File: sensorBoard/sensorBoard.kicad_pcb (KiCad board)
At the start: 2 copper layers, 150 x 100 mm, 92 parts, among them J1 Conn_01x04, J2 Conn_01x02, J3 Conn_01x07, J4 Conn_01x04, J5 Conn_01x05, J6 Conn_01x02, J7 Conn_01x02, J8 Conn_01x03, K3 G2RL-1-H, K4 G2RL-1-H, Q1 NTD3055, Q2 2N7002, Q3 2SC4213, Q4 BSC440N10NS3G, Q5 BSC440N10NS3G, Q6 BSC440N10NS3G, Q7 BSC440N10NS3G, Q8 2N7002, Q9 2N7002, U1 STM32L476RGTx, U10 4N25, U11 4N25, U12 4011, U14 4011, U2 LD1117S33TR_SOT223, U3 MCP2551-I-SN, U4 LM75C, U6 4011, U7 BTS50080-1TEA, U8 4011, Y1 8MHz

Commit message: started to connect layout. added 0 Ohm resistors to separate the drivers.
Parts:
- added D7: ESD9B3.3ST5G, Diode_SMD:D_SOD-523, F.Cu at (79.0, 124.0)
- added R20: 0, Resistor_SMD:R_0805_2012Metric, F.Cu at (132.0, 53.2)
- added R21: 0, Resistor_SMD:R_0805_2012Metric, F.Cu at (132.1, 57.0)
- added R23: 0, Resistor_SMD:R_0805_2012Metric, F.Cu at (132.1, 60.3)
- added R24: 0, Resistor_SMD:R_0805_2012Metric, F.Cu at (132.1, 63.5)
- added R25: 0, Resistor_SMD:R_0805_2012Metric, F.Cu at (45.7, 75.0)
- added R30: 0, Resistor_SMD:R_0805_2012Metric, F.Cu at (64.2, 53.0)
- added R31: 0, Resistor_SMD:R_0805_2012Metric, F.Cu at (64.8, 79.5)
- added R32: 0, Resistor_SMD:R_0805_2012Metric, F.Cu at (77.2, 76.2)
- U10, U11: footprint Package_DIP:DIP-6_W7.62mm -> Package_DIP:SMDIP-6_W9.53mm_Clearance8mm
- moved U4 253.1 mm to (93.0, 104.0)
- moved Q3 247.8 mm to (92.0, 109.0)
- moved C4 242.7 mm to (98.0, 102.0)
- moved R2 240.5 mm to (101.0, 111.8)
- moved R3 240.4 mm to (96.9, 108.0)
- moved R1 240.1 mm to (101.0, 108.0), turned to 180 degrees
- moved R4 239.4 mm to (101.0, 115.5), turned to 180 degrees
- moved D8 235.3 mm to (58.0, 75.0), turned to 90 degrees
- moved R8 235.2 mm to (106.1, 100.0), turned to 180 degrees
- moved R10 234.3 mm to (106.0, 104.0), turned to 180 degrees
- moved R12 233.3 mm to (106.0, 108.0), turned to 180 degrees
- moved U13 232.5 mm to (116.0, 109.0)
- moved R9 232.5 mm to (110.0, 104.0), turned to 180 degrees
- moved R26 232.4 mm to (89.0, 88.0)
- moved R11 231.4 mm to (110.0, 108.0), turned to 180 degrees
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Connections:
- K3 pad 11: /Commutation/POLE+ -> /Commutation/Motor_driver_1/POLE1
- K4 pad 11: /Commutation/POLE- -> /Commutation/Motor_driver_1/POLE2
- Q4 pad 1: /Commutation/POLE+ -> /Commutation/Motor_driver_2/POLE_1
- Q4 pad 2: /Commutation/POLE+ -> /Commutation/Motor_driver_2/POLE_1
- Q4 pad 3: /Commutation/POLE+ -> /Commutation/Motor_driver_2/POLE_1
- Q5 pad 1: /Commutation/POLE- -> /Commutation/Motor_driver_2/POLE_2
- Q5 pad 2: /Commutation/POLE- -> /Commutation/Motor_driver_2/POLE_2
- Q5 pad 3: /Commutation/POLE- -> /Commutation/Motor_driver_2/POLE_2
- Q6 pad 5: /Commutation/POLE+ -> /Commutation/Motor_driver_2/POLE_1
- Q7 pad 5: /Commutation/POLE- -> /Commutation/Motor_driver_2/POLE_2
- U12 pad 10: unconnected-(U12-Pad10) -> Net-(U12-Pad10)
- U12 pad 12: Net-(U12-Pad12) -> Net-(U12-Pad10)
- U12 pad 13: Net-(U12-Pad12) -> Net-(U12-Pad10)
- U12 pad 14: +5V -> +12V
- U12 pad 8: unconnected-(U12-Pad8) -> Net-(U12-Pad3)
- U12 pad 9: unconnected-(U12-Pad9) -> Net-(U15-2Y)
- U14 pad 10: Net-(U12-Pad12) -> unconnected-(U14-Pad10)
- U14 pad 14: +5V -> +12V
- U14 pad 8: Net-(U12-Pad3) -> unconnected-(U14-Pad8)
- U14 pad 9: Net-(U15-2Y) -> unconnected-(U14-Pad9)
- U15 pad 1: /DIN -> /Commutation/Motor_driver_1/DIN
- U15 pad 3: /EN_MOTOR -> /Commutation/Motor_driver_1/EN_MOTOR
- U5 pad 1: /DIN -> /Commutation/Motor_driver_2/DIN
- U5 pad 3: /EN_MOTOR -> /Commutation/Motor_driver_2/EN_MOTOR
- U6 pad 14: +5V -> +12V
- U8 pad 14: +5V -> +12V
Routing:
- net Net-(U5-2Y): track 0.00 -> 81.9 mm, vias 0 -> 6
- net Net-(U5-1Y): track 0.00 -> 53.9 mm, vias 0 -> 2
- net Net-(Q6-G): track 0.00 -> 50.7 mm, vias 0 -> 2
- net Net-(U15-1Y): track 0.00 -> 31.7 mm, vias 0 -> 2
- net +3.3V: track 0.00 -> 30.6 mm
- net Net-(U15-2Y): track 0.00 -> 30.3 mm, vias 0 -> 2
- net Net-(U12-Pad4): track 0.00 -> 27.8 mm, vias 0 -> 2
- net Net-(Q4-G): track 0.00 -> 27.4 mm, vias 0 -> 2
- net Net-(Q7-G): track 0.00 -> 26.6 mm, vias 0 -> 2
- net Net-(Q5-G): track 0.00 -> 24.0 mm, vias 0 -> 2
- net Net-(Q1-G): track 0.00 -> 21.1 mm
- net Net-(U1-PH1): track 0.00 -> 18.1 mm
- net Net-(U11-Pad2): track 0.00 -> 17.4 mm, vias 0 -> 2
- net Net-(U10-Pad2): track 0.00 -> 17.0 mm, vias 0 -> 2
- net Net-(U1-PH0): track 0.00 -> 16.8 mm
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- added copper zone on F.Cu, net +12V
- added copper zone on F.Cu, net +5V
- added copper zone on F.Cu, net /Commutation/LAMP_OUT
- added copper zone on F.Cu, net /Commutation/Motor_driver_1/POLE2
- added copper zone on F.Cu, net /Commutation/Motor_driver_2/POLE_1
- added copper zone on F.Cu, net /Commutation/Motor_driver_2/POLE_2
- added copper zone on F.Cu, net /Commutation/POLE+
- added copper zone on F.Cu, net /Commutation/POLE-
- added copper zone on F.Cu, net /Commutation/SERVO_OUT
- added copper zone on F.Cu, net /Protection/12V_IN
- added copper zone on F.Cu, net /Protection/5V_IN
- added copper zone on F.Cu, net Net-(F1-Pad2)
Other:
- copper layers 2 -> 4

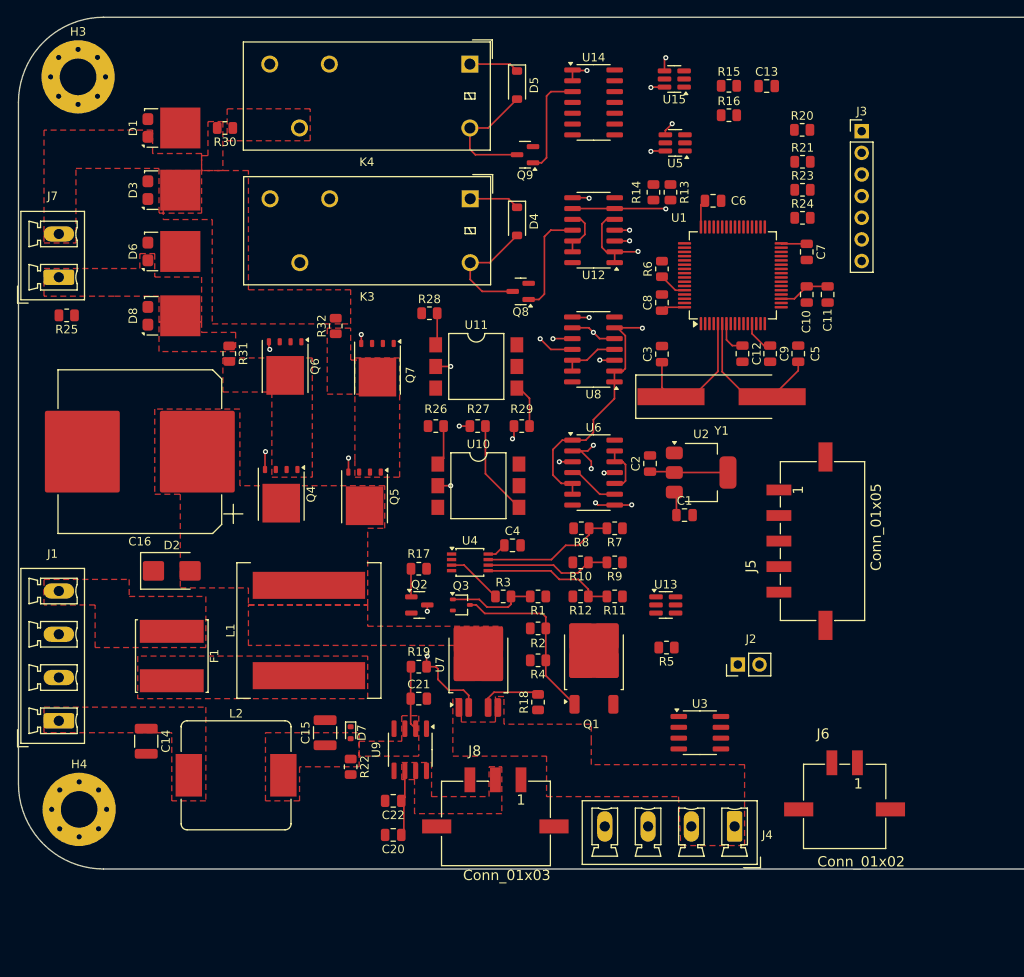
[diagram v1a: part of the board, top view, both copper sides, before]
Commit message: Die Platine mit den allen Komponenten auf einziges PCB
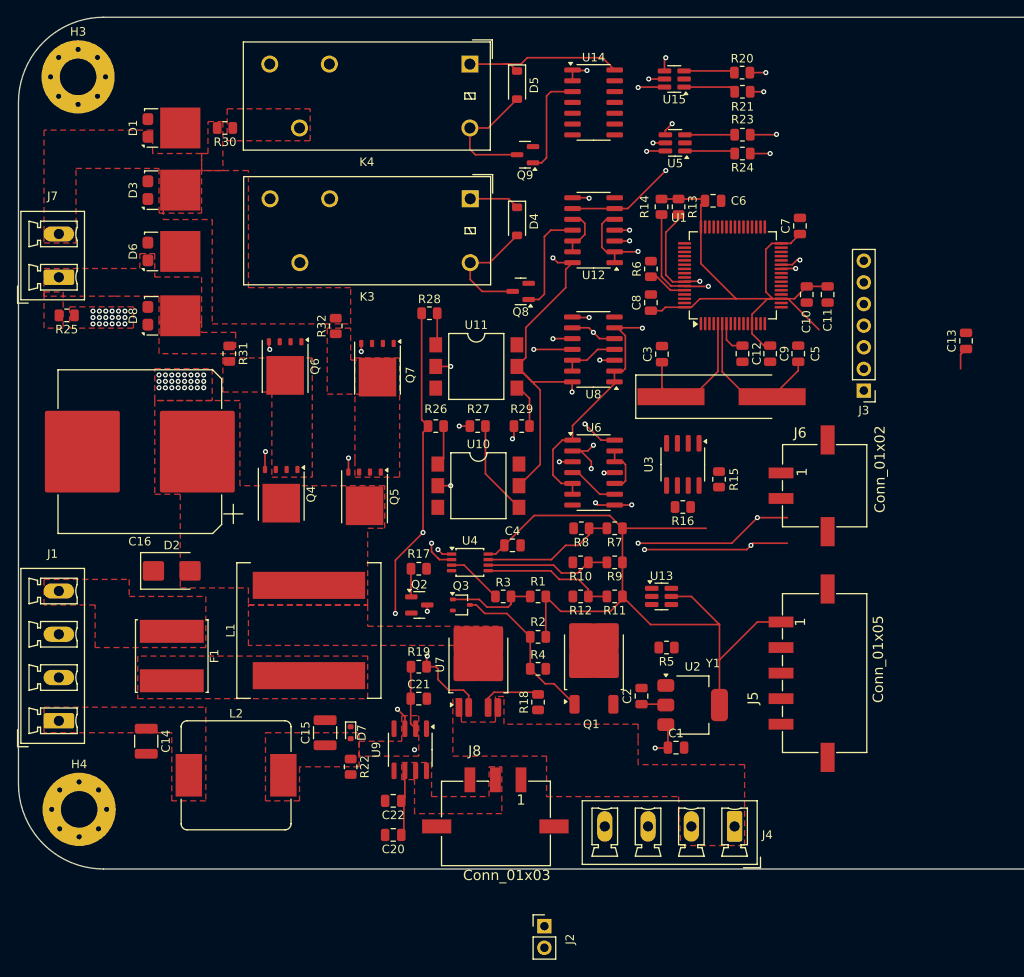
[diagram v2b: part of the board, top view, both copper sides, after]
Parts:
- moved R16 46.3 mm to (118.0, 97.5), turned to 180 degrees
- moved R15 46.2 mm to (122.2, 94.2), turned to 90 degrees
- moved J2 38.2 mm to (101.8, 146.7), turned to 0 degrees
- moved J6 38.1 mm to (135.0, 95.0), turned to 90 degrees
- moved C13 38.0 mm to (151.2, 78.0), turned to 90 degrees
- moved U3 31.6 mm to (118.0, 92.5), turned to -90 degrees
- moved J3 30.5 mm to (139.2, 83.8), turned to 180 degrees
- moved C1 27.3 mm to (117.2, 125.8)
- moved C2 27.3 mm to (113.2, 119.7)
- moved U2 27.3 mm to (119.2, 120.8)
- moved J5 15.5 mm to (135.0, 117.0)
- moved R21 10.8 mm to (125.0, 48.8)
- moved R24 10.3 mm to (125.0, 56.0), turned to 180 degrees
- moved R20 9.74 mm to (125.0, 46.5)
- moved R23 9.57 mm to (125.0, 53.8), turned to 180 degrees
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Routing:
- net +5V: track 10.4 -> 173.7 mm, vias 0 -> 7
- net +3.3V: track 30.6 -> 158.2 mm
- net /I2C_SCL: track 0.00 -> 92.0 mm, vias 0 -> 4
- net /I2C_SDA: track 0.00 -> 90.7 mm, vias 0 -> 4
- net +12V: track 11.8 -> 90.7 mm, vias 0 -> 27
- net /EN_MOTOR: track 0.00 -> 31.4 mm, vias 0 -> 3
- net /DIN: track 0.00 -> 27.9 mm, vias 0 -> 3
- net /Commutation/Motor_driver_1/DIN: track 0.00 -> 6.17 mm
- net /Commutation/Motor_driver_1/EN_MOTOR: track 0.00 -> 5.98 mm
- net /Commutation/Motor_driver_2/DIN: track 0.00 -> 5.96 mm
- net /Commutation/Motor_driver_2/EN_MOTOR: track 0.00 -> 5.84 mm
- net Net-(U15-2Y): track 30.3 -> 27.7 mm
- net Net-(Q1-G): track 21.1 -> 19.3 mm
- net Net-(U1-BOOT0): track 3.31 -> 4.61 mm
- net Net-(U15-1Y): track 31.7 -> 32.6 mm
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- added copper zone on In2.Cu, net +12V
- added copper zone on F.Cu, net /Commutation/Motor_driver_1/POLE1
- added copper zone on In2.Cu, net /Commutation/Motor_driver_1/POLE1

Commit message: new two separate pcbs
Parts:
- removed C1, C10, C12, C13, C4, C6, C7, C8, C9: 0.1µF, Capacitor_SMD:C_0805_2012Metric
- removed C11: 4.7µF, Capacitor_SMD:C_0805_2012Metric
- removed C14, C15: 10µF, Capacitor_SMD:C_1210_3225Metric
- removed C16: 2200µF, Capacitor_SMD:CP_Elec_18x17.5
- removed C2: 10µF, Capacitor_SMD:C_0805_2012Metric
- removed C22: 22µF, Capacitor_SMD:C_0805_2012Metric
- removed C3, C5: 20pF, Capacitor_SMD:C_0805_2012Metric
- removed D7: ESD9B3.3ST5G, Diode_SMD:D_SOD-523
- removed F1: Fuse_Small, Inductor_SMD:L_Cenker_CKCS8080
- removed H1, H2, H3, H4: MountingHole_Pad, MountingHole:MountingHole_4.3mm_M4_Pad_Via
- removed J1, J4: Conn_01x04, Connector_Phoenix_MC_HighVoltage:PhoenixContact_MCV_1,5_4-G-5.08_1x04_P5.08mm_Vertical
- removed J2: Conn_01x02, Connector_PinHeader_2.54mm:PinHeader_1x02_P2.54mm_Vertical
- removed J3: Conn_01x07, Connector_PinHeader_2.54mm:PinHeader_1x07_P2.54mm_Vertical
- removed J5: Conn_01x05, heder box:662105145021
- removed J6: Conn_01x02, heder box:662102145021
- removed J7: Conn_01x02, Connector_Phoenix_MC_HighVoltage:PhoenixContact_MCV_1,5_2-G-5.08_1x02_P5.08mm_Vertical
- removed J8: Conn_01x03, heder box:662103145021
- removed K3, K4: G2RL-1-H, Relay_THT:Relay_SPDT_Omron_G2RL-1
- removed L1: 10µH, Inductor_SMD:L_Coilcraft_XAL1580-612
- removed L2: 10µH, Inductor_SMD:L_Bourns_SRP1245A
- removed Q1: NTD3055, Package_TO_SOT_SMD:TO-252-2
- removed Q3: 2SC4213, Package_TO_SOT_SMD:SOT-323_SC-70
- removed Q4, Q5, Q6, Q7: BSC440N10NS3G, Package_TO_SOT_SMD:TDSON-8-1
- removed Q8, Q9: 2N7002, Package_TO_SOT_SMD:SOT-23
- removed R10, R12, R13, R14, R8: 10k, Resistor_SMD:R_0805_2012Metric
- removed R11, R7, R9: N.P., Resistor_SMD:R_0805_2012Metric
- removed R15: R_Small, Resistor_SMD:R_0805_2012Metric
- removed R16: 120, Resistor_SMD:R_0805_2012Metric
- removed R18: 1k, Resistor_SMD:R_0805_2012Metric
- removed R19, R27, R29: 100, Resistor_SMD:R_0805_2012Metric
- removed R25, R30, R31, R32: 0, Resistor_SMD:R_0805_2012Metric
- removed R26, R28: 380, Resistor_SMD:R_0805_2012Metric
- removed U1: STM32L476RGTx, Package_QFP:LQFP-64_10x10mm_P0.5mm
- removed U10, U11: 4N25, Package_DIP:SMDIP-6_W9.53mm_Clearance8mm
- removed U13, U15, U5: ~, Package_TO_SOT_SMD:SC-74-6_1.55x2.9mm_P0.95mm
- removed U14, U6, U8: 4011, Package_SO:SOIC-14_3.9x8.7mm_P1.27mm
- removed U2: LD1117S33TR_SOT223, Package_TO_SOT_SMD:SOT-223-3_TabPin2
- removed U3: MCP2551-I-SN, Package_SO:SOIC-8_3.9x4.9mm_P1.27mm
- removed U4: LM75C, Package_SO:TSSOP-8_3x3mm_P0.65mm
- removed Y1: 8MHz, Crystal:Crystal_SMD_HC49-SD_HandSoldering
- added C17: 0.1µF, Capacitor_SMD:C_0805_2012Metric, F.Cu at (107.9, 117.9)
- added C18: 0.1µF, Capacitor_SMD:C_0805_2012Metric, F.Cu at (96.8, 111.9)
- added C19: 10µF, Capacitor_SMD:C_0805_2012Metric, F.Cu at (104.6, 107.5)
- added C23: 0.1µF, Capacitor_SMD:C_0805_2012Metric, F.Cu at (60.0, 129.0)
- added C24: 0.1µF, Capacitor_SMD:C_0805_2012Metric, F.Cu at (50.0, 133.0)
- added C25: 22µF, Capacitor_SMD:C_0805_2012Metric, F.Cu at (50.0, 136.0)
- added C26: 10µF, Capacitor_SMD:C_1210_3225Metric, F.Cu at (65.0, 115.1)
- added C27: 2200µF, Capacitor_SMD:CP_Elec_18x17.5, F.Cu at (80.9, 100.8)
- added C28: 10µF, Capacitor_SMD:C_1210_3225Metric, F.Cu at (66.6, 124.0)
- added C29: 0.1µF, Capacitor_SMD:C_0805_2012Metric, F.Cu at (106.7, 64.1)
- added C30: 0.1µF, Capacitor_SMD:C_0805_2012Metric, F.Cu at (102.1, 94.3)
- added C31: 20pF, Capacitor_SMD:C_0805_2012Metric, F.Cu at (102.1, 84.6)
- added C32: 20pF, Capacitor_SMD:C_0805_2012Metric, F.Cu at (102.1, 98.3)
- added C33: 0.1µF, Capacitor_SMD:C_0805_2012Metric, F.Cu at (106.7, 82.1)
- added C34: 0.1µF, Capacitor_SMD:C_0805_2012Metric, F.Cu at (104.4, 98.2)
- added C35: 0.1µF, Capacitor_SMD:C_0805_2012Metric, F.Cu at (108.9, 100.6)
- added C36: 0.1µF, Capacitor_SMD:C_0805_2012Metric, F.Cu at (120.6, 86.9)
- added C37: 0.1µF, Capacitor_SMD:C_0805_2012Metric, F.Cu at (118.8, 99.6)
- added C38: 4.7µF, Capacitor_SMD:C_0805_2012Metric, F.Cu at (108.9, 103.3)
- added C39: 0.1µF, Capacitor_SMD:C_0805_2012Metric, F.Cu at (423.5, 18.7)
- added C40: 0.1µF, Capacitor_SMD:C_0805_2012Metric, F.Cu at (408.2, 118.6)
- added C41: 0.1µF, Capacitor_SMD:C_0805_2012Metric, F.Cu at (408.2, 121.6)
- added C42: 22µF, Capacitor_SMD:C_0805_2012Metric, F.Cu at (408.2, 124.6)
- added C43: 10µF, Capacitor_SMD:C_1210_3225Metric, F.Cu at (176.7, 71.6)
- added C44: 2200µF, Capacitor_SMD:CP_Elec_18x17.5, F.Cu at (153.3, 84.5)
- added C45: 10µF, Capacitor_SMD:C_1210_3225Metric, F.Cu at (176.7, 78.9)
- added C46: 0.1µF, Capacitor_SMD:C_0805_2012Metric, F.Cu at (434.9, 101.4)
- added C47: 0.1µF, Capacitor_SMD:C_0805_2012Metric, F.Cu at (406.1, 64.2)
- added C48: 20pF, Capacitor_SMD:C_0805_2012Metric, F.Cu at (406.1, 67.2)
- added C49: 20pF, Capacitor_SMD:C_0805_2012Metric, F.Cu at (406.1, 70.2)
- added C50: 0.1µF, Capacitor_SMD:C_0805_2012Metric, F.Cu at (410.5, 64.2)
- added C51: 0.1µF, Capacitor_SMD:C_0805_2012Metric, F.Cu at (410.5, 67.2)
- added C52: 0.1µF, Capacitor_SMD:C_0805_2012Metric, F.Cu at (410.5, 70.2)
- added C53: 0.1µF, Capacitor_SMD:C_0805_2012Metric, F.Cu at (415.0, 64.2)
- added C54: 0.1µF, Capacitor_SMD:C_0805_2012Metric, F.Cu at (415.0, 67.2)
- added C55: 4.7µF, Capacitor_SMD:C_0805_2012Metric, F.Cu at (415.0, 70.2)
- added D10: D_KAA, Package_TO_SOT_SMD:TO-277A, F.Cu at (46.0, 86.0)
- added D11: D_KAA, Package_TO_SOT_SMD:TO-277A, F.Cu at (46.0, 60.0)
- added D12: D_KAA, Package_TO_SOT_SMD:TO-277A, F.Cu at (46.0, 68.0)
- added D13: ESD9B3.3ST5G, Diode_SMD:D_SMB, F.Cu at (44.4, 94.8)
- added D14: ESD9B3.3ST5G, Diode_SMD:D_SOD-523, F.Cu at (61.0, 124.7)
- added D17: D_KAA, Package_TO_SOT_SMD:TO-277A, F.Cu at (398.9, 112.9)
- added D18: D_KAA, Package_TO_SOT_SMD:TO-277A, F.Cu at (405.3, 112.9)
- added D19: D_KAA, Package_TO_SOT_SMD:TO-277A, F.Cu at (411.6, 112.9)
- added D20: ESD9B3.3ST5G, Diode_SMD:D_SMB, F.Cu at (168.9, 66.6)
- added D21: ESD9B3.3ST5G, Diode_SMD:D_SOD-523, F.Cu at (170.2, 77.0)
- added D22: D_Small, Diode_SMD:D_SOD-123, F.Cu at (87.0, 76.8)
- added D23: D_Small, Diode_SMD:D_SOD-123, F.Cu at (87.1, 54.0)
- added D9: D_KAA, Package_TO_SOT_SMD:TO-277A, F.Cu at (46.0, 78.0)
- added F2: Fuse_Small, Inductor_SMD:L_Cenker_CKCS8080, F.Cu at (44.0, 104.0)
- added F3: Fuse_Small, Inductor_SMD:L_Cenker_CKCS8080, F.Cu at (169.7, 57.5)
- added H10: MountingHole_Pad, MountingHole:MountingHole_4.3mm_M4_Pad_Via, F.Cu at (40.2, 50.0)
- added H11: MountingHole_Pad, MountingHole:MountingHole_4.3mm_M4_Pad_Via, F.Cu at (119.9, 129.9)
- added H12: MountingHole_Pad, MountingHole:MountingHole_4.3mm_M4_Pad_Via, F.Cu at (40.0, 129.9)
- added H5: MountingHole_Pad, MountingHole:MountingHole_4.3mm_M4_Pad_Via, F.Cu at (370.5, 15.7)
- added H6: MountingHole_Pad, MountingHole:MountingHole_4.3mm_M4_Pad_Via, F.Cu at (370.5, 25.8)
- added H7: MountingHole_Pad, MountingHole:MountingHole_4.3mm_M4_Pad_Via, F.Cu at (370.5, 36.0)
- added H8: MountingHole_Pad, MountingHole:MountingHole_4.3mm_M4_Pad_Via, F.Cu at (370.5, 46.1)
- added H9: MountingHole_Pad, MountingHole:MountingHole_4.3mm_M4_Pad_Via, F.Cu at (119.9, 50.0)
- added J10: Conn_01x07, Connector_PinHeader_2.54mm:PinHeader_1x07_P2.54mm_Vertical, F.Cu at (127.4, 81.3)
- added J11: Conn_01x03, heder box:662103145021, F.Cu at (72.0, 135.0)
- added J12: Conn_01x02, heder box:662102145021, F.Cu at (125.2, 113.0)
- added J13: Conn_01x04, Connector_Phoenix_MC_HighVoltage:PhoenixContact_MCV_1,5_4-G-5.08_1x04_P5.08mm_Vertical, F.Cu at (101.6, 135.3)
- added J14: Conn_01x05, heder box:662105145021, F.Cu at (124.7, 65.2)
- added J15: Conn_01x02, Connector_Phoenix_MC_HighVoltage:PhoenixContact_MCV_1,5_2-G-5.08_1x02_P5.08mm_Vertical, F.Cu at (34.7, 74.5)
- added J16: Conn_01x02, Connector_PinHeader_2.54mm:PinHeader_1x02_P2.54mm_Vertical, F.Cu at (83.3, 43.4)
- added J17: Conn_01x04, Connector_Phoenix_MC_HighVoltage:PhoenixContact_MCV_1,5_4-G-5.08_1x04_P5.08mm_Vertical, F.Cu at (156.2, 71.3)
- added J18: Conn_01x07, Connector_PinHeader_2.54mm:PinHeader_1x07_P2.54mm_Vertical, F.Cu at (323.0, 17.5)
- added J19: Conn_01x03, heder box:662103145021, F.Cu at (337.8, 36.7)
- added J20: Conn_01x02, heder box:662102145021, F.Cu at (354.5, 36.7)
- added J21: Conn_01x04, Connector_Phoenix_MC_HighVoltage:PhoenixContact_MCV_1,5_4-G-5.08_1x04_P5.08mm_Vertical, F.Cu at (332.3, 26.7)
- added J22: Conn_01x05, heder box:662105145021, F.Cu at (340.8, 49.3)
- added J23: Conn_01x02, Connector_Phoenix_MC_HighVoltage:PhoenixContact_MCV_1,5_2-G-5.08_1x02_P5.08mm_Vertical, F.Cu at (338.5, 14.7)
- added J24: Conn_01x02, Connector_PinHeader_2.54mm:PinHeader_1x02_P2.54mm_Vertical, F.Cu at (430.4, 93.0)
- added J9: Conn_01x04, Connector_Phoenix_MC_HighVoltage:PhoenixContact_MCV_1,5_4-G-5.08_1x04_P5.08mm_Vertical, F.Cu at (35.1, 117.7)
- added K5: G2RL-1-H, Relay_THT:Relay_SPDT_Omron_G2RL-1, F.Cu at (82.0, 73.3)
- added K6: G2RL-1-H, Relay_THT:Relay_SPDT_Omron_G2RL-1, F.Cu at (82.0, 50.3)
- added L3: 10µH, Inductor_SMD:L_Coilcraft_XAL1580-612, F.Cu at (58.4, 101.0)
- added L4: 10µH, Inductor_SMD:L_Bourns_SRP1245A, F.Cu at (53.0, 118.5)
- added L5: 10µH, Inductor_SMD:L_Coilcraft_XAL1580-612, F.Cu at (185.6, 59.2)
- added L6: 10µH, Inductor_SMD:L_Bourns_SRP1245A, F.Cu at (188.2, 75.9)
- added Q10: 2N7002, Package_TO_SOT_SMD:SOT-23, F.Cu at (82.0, 123.8)
- added Q11: 2SC4213, Package_TO_SOT_SMD:SOT-323_SC-70, F.Cu at (112.9, 61.0)
- added Q12: NTD3055, Package_TO_SOT_SMD:TO-252-2, F.Cu at (95.2, 48.4)
- added Q19: 2SC4213, Package_TO_SOT_SMD:SOT-323_SC-70, F.Cu at (430.3, 99.9)
- added Q20: NTD3055, Package_TO_SOT_SMD:TO-252-2, F.Cu at (434.9, 86.6)
- added Q21: 2N7002, Package_TO_SOT_SMD:SOT-23, F.Cu at (88.0, 81.8)
- added Q22: 2N7002, Package_TO_SOT_SMD:SOT-23, F.Cu at (88.1, 59.0)
- added Q23: BSC440N10NS3G, Package_TO_SOT_SMD:TDSON-8-1, F.Cu at (358.5, 102.6)
- added Q24: BSC440N10NS3G, Package_TO_SOT_SMD:TDSON-8-1, F.Cu at (358.5, 109.4)
- added Q25: BSC440N10NS3G, Package_TO_SOT_SMD:TDSON-8-1, F.Cu at (358.5, 116.1)
- added Q26: BSC440N10NS3G, Package_TO_SOT_SMD:TDSON-8-1, F.Cu at (358.5, 122.8)
- added R33: R_Small, Resistor_SMD:R_0805_2012Metric, F.Cu at (115.5, 108.2)
- added R34: 120, Resistor_SMD:R_0805_2012Metric, F.Cu at (115.5, 112.6)
- added R35: 100, Resistor_SMD:R_0805_2012Metric, F.Cu at (78.1, 123.9)
- added R36: 100, Resistor_SMD:R_0805_2012Metric, F.Cu at (86.1, 123.9)
- added R37: 10k, Resistor_SMD:R_0805_2012Metric, F.Cu at (51.0, 130.0)
- added R38: 1k, Resistor_SMD:R_0805_2012Metric, F.Cu at (74.4, 123.9)
- added R41: 0, Resistor_SMD:R_0805_2012Metric, F.Cu at (425.8, 84.1)
- added R42: 10k, Resistor_SMD:R_0805_2012Metric, F.Cu at (425.8, 87.0)
- added R43: 10k, Resistor_SMD:R_0805_2012Metric, F.Cu at (425.8, 90.0)
- added R44: 0, Resistor_SMD:R_0805_2012Metric, F.Cu at (425.8, 92.9)
- added R46: 10k, Resistor_SMD:R_0805_2012Metric, F.Cu at (406.1, 73.2)
- added R53: 0, Resistor_SMD:R_0805_2012Metric, F.Cu at (106.7, 67.0)
- added R54: 10k, Resistor_SMD:R_0805_2012Metric, F.Cu at (106.7, 69.6)
- added R55: 10k, Resistor_SMD:R_0805_2012Metric, F.Cu at (106.7, 72.0)
- added R56: 0, Resistor_SMD:R_0805_2012Metric, F.Cu at (110.8, 46.1)
- added R58: 10k, Resistor_SMD:R_0805_2012Metric, F.Cu at (106.7, 79.6)
- added R59: 10k, Resistor_SMD:R_0805_2012Metric, F.Cu at (106.7, 74.5)
- added R60: 10k, Resistor_SMD:R_0805_2012Metric, F.Cu at (106.7, 77.1)
- added R65: 10k, Resistor_SMD:R_0805_2012Metric, F.Cu at (406.1, 76.2)
- added R66: 10k, Resistor_SMD:R_0805_2012Metric, F.Cu at (406.1, 79.1)
- added R67: 380, Resistor_SMD:R_0805_2012Metric, F.Cu at (377.4, 100.8)
- added R68: 380, Resistor_SMD:R_0805_2012Metric, F.Cu at (377.4, 103.7)
- added R69: 100, Resistor_SMD:R_0805_2012Metric, F.Cu at (377.4, 106.7)
- added R70: 100, Resistor_SMD:R_0805_2012Metric, F.Cu at (377.4, 109.6)
- added U17: LD1117S33TR_SOT223, Package_TO_SOT_SMD:SOT-223-3_TabPin2, F.Cu at (98.9, 106.6)
- added U19: ~, Package_SO:SOIC-8_3.9x4.9mm_P1.27mm, F.Cu at (55.0, 132.0)
- added U20: BTS50080-1TEA, Package_TO_SOT_SMD:TO-252-4, F.Cu at (78.6, 116.5)
- added U21: LM75C, Package_SO:TSSOP-8_3x3mm_P0.65mm, F.Cu at (106.8, 60.8)
- added U22: ~, Package_TO_SOT_SMD:SC-74-6_1.55x2.9mm_P0.95mm, F.Cu at (106.3, 45.9)
- added U23: STM32L476RGTx, Package_QFP:LQFP-64_10x10mm_P0.5mm, F.Cu at (112.3, 92.2)
- added U31: ~, Package_SO:SOIC-8_3.9x4.9mm_P1.27mm, F.Cu at (393.6, 128.5)
- added U32: BTS50080-1TEA, Package_TO_SOT_SMD:TO-252-4, F.Cu at (396.3, 121.1)
- added U33: LM75C, Package_SO:TSSOP-8_3x3mm_P0.65mm, F.Cu at (436.2, 93.0)
- added U34: ~, Package_TO_SOT_SMD:SC-74-6_1.55x2.9mm_P0.95mm, F.Cu at (435.4, 97.7)
- added U35: STM32L476RGTx, Package_QFP:LQFP-64_10x10mm_P0.5mm, F.Cu at (396.6, 69.9)
- added U36: 4011, Package_SO:SOIC-14_3.9x8.7mm_P1.27mm, F.Cu at (96.5, 76.2)
- added U37: ~, Package_TO_SOT_SMD:SC-74-6_1.55x2.9mm_P0.95mm, F.Cu at (106.3, 52.6)
- added U38: 4011, Package_SO:SOIC-14_3.9x8.7mm_P1.27mm, F.Cu at (96.5, 62.8)
- added U39: 4011, Package_SO:SOIC-14_3.9x8.7mm_P1.27mm, F.Cu at (366.8, 123.0)
- added U40: 4011, Package_SO:SOIC-14_3.9x8.7mm_P1.27mm, F.Cu at (375.3, 123.0)
- added U41: ~, Package_TO_SOT_SMD:SC-74-6_1.55x2.9mm_P0.95mm, F.Cu at (378.0, 113.5)
- added U42: 4N25, Package_DIP:SMDIP-6_W9.53mm_Clearance8mm, F.Cu at (368.9, 103.9)
- added U43: 4N25, Package_DIP:SMDIP-6_W9.53mm_Clearance8mm, F.Cu at (368.9, 113.2)
- added Y2: 8MHz, Crystal:Crystal_SMD_HC49-SD_HandSoldering, F.Cu at (97.7, 91.4)
- added Y3: 8MHz, Crystal:Crystal_SMD_HC49-SD_HandSoldering, F.Cu at (400.1, 59.6)
- C21: value 0.1µF -> 10µF
- D1, D3, D6: value D_KAA -> LED_Small; footprint Package_TO_SOT_SMD:TO-277A -> LED_SMD:LED_0805_2012Metric
- D2: value ESD9B3.3ST5G -> LED_Small; footprint Diode_SMD:D_SMB -> LED_SMD:LED_0805_2012Metric
- D4, D5: value D_Small -> LED_Small; footprint Diode_SMD:D_SOD-123 -> LED_SMD:LED_0805_2012Metric
- R1, R2, R4, R6: value 10k -> 1k
- R17: value 100 -> R_Small
- R20: value 0 -> 120
- R21: value 0 -> 100
- R22: value 10k -> 100
- R23: value 0 -> 10k
- R24, R3, R5: value 0 -> 1k
- U12: value 4011 -> MCP2551-I-SN; footprint Package_SO:SOIC-14_3.9x8.7mm_P1.27mm -> Package_SO:SOIC-8_3.9x4.9mm_P1.27mm
- U7: value BTS50080-1TEA -> LD1117S33TR_SOT223; footprint Package_TO_SOT_SMD:TO-252-4 -> Package_TO_SOT_SMD:SOT-223-3_TabPin2
- U9: value ~ -> MCP2551-I-SN
- moved U9 353.3 mm to (421.0, 14.0), turned to 0 degrees
- moved R17 343.0 mm to (419.0, 18.7), turned to 0 degrees
- moved D8 336.8 mm to (392.6, 112.9), turned to 0 degrees
- moved R22 324.8 mm to (403.8, 121.5), turned to 0 degrees
- moved Q2 321.9 mm to (408.4, 128.5)
- moved R20 295.1 mm to (419.0, 21.6)
- moved R24 287.8 mm to (403.8, 127.4), turned to 0 degrees
- moved R23 287.6 mm to (403.8, 124.4), turned to 0 degrees
- moved R21 287.4 mm to (403.8, 118.5)
- moved C20 286.5 mm to (355.2, 43.4), turned to 0 degrees
- moved C21 278.1 mm to (355.2, 46.4)
- moved U7 277.7 mm to (356.1, 24.1), turned to 0 degrees
- moved D2 159.8 mm to (167.3, -11.5)
- moved R4 143.7 mm to (171.7, -8.57)
- moved R2 143.0 mm to (171.7, -11.5), turned to 0 degrees
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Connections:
- C20 pad 1: /Commutation/SERVO_OUT -> +5V
- C21 pad 1: +5V -> +3.3V
- D1 pad 1: /Commutation/POLE- -> Net-(D1-K)
- D1 pad 2: unconnected-(D1-A-Pad2) -> Net-(D1-A)
- D2 pad 1: GND -> Net-(D2-K)
- D2 pad 2: +12V -> Net-(D2-A)
- D3 pad 1: +12V -> Net-(D3-K)
- D3 pad 2: unconnected-(D3-A-Pad2) -> Net-(D3-A)
- D4 pad 1: +12V -> Net-(D4-K)
- D5 pad 1: +12V -> Net-(D5-K)
- D6 pad 1: /Commutation/POLE+ -> Net-(D6-K)
- D6 pad 2: unconnected-(D6-A-Pad2) -> Net-(D6-A)
- D8 pad 3: /Commutation/POLE+ -> /Platine2/Commutation2-2/POLE+
- R1 pad 1: +3.3V -> Net-(D1-K)
- R1 pad 2: Net-(Q3-B) -> GND
- R17 pad 1: /LED_EN -> Net-(U9-Rs)
- R17 pad 2: Net-(Q2-G) -> GND
- R2 pad 1: +3.3V -> Net-(D2-K)
- R2 pad 2: Net-(Q1-G) -> GND
- R20 pad 1: /Commutation/Motor_driver_1/EN_MOTOR -> /Platine2/CAN_H
- R20 pad 2: /EN_MOTOR -> /Platine2/CAN_L
- R21 pad 1: /Commutation/Motor_driver_1/DIN -> /Platine2/LED_EN
- R21 pad 2: /DIN -> Net-(Q2-G)
- R22 pad 1: +5V -> Net-(Q2-D)
- R22 pad 2: /Commutation/OVER_CURR_SERVO -> +5V
- R23 pad 1: /EN_MOTOR -> +5V
- R23 pad 2: /Commutation/Motor_driver_2/EN_MOTOR -> /Platine2/Commutation2-2/OVER_CURR_SERVO
- R24 pad 1: /DIN -> GND
- R24 pad 2: /Commutation/Motor_driver_2/DIN -> /Platine2/IS_DIAG
- R3 pad 1: Net-(U4-O.S.) -> Net-(D3-K)
- R3 pad 2: Net-(Q3-B) -> GND
- R4 pad 1: Net-(Q1-G) -> Net-(D4-K)
- R5 pad 1: Net-(U13-1Y) -> Net-(D5-K)
- R5 pad 2: Net-(Q1-G) -> GND
- R6 pad 1: Net-(U1-BOOT0) -> Net-(D6-K)
- U12 pad 1: Net-(U15-1Y) -> /Platine1/CanTransceiver1/CAN_TX
- U12 pad 2: Net-(U15-1Y) -> GND
- U12 pad 3: Net-(U12-Pad3) -> +5V
- U12 pad 4: Net-(U12-Pad4) -> /Platine1/CanTransceiver1/CAN_RX
- U12 pad 5: Net-(U15-1Y) -> unconnected-(U12-Vref-Pad5)
- U12 pad 6: Net-(U15-2Y) -> /Platine1/CAN_L
- U12 pad 7: GND -> /Platine1/CAN_H
- U12 pad 8: Net-(U12-Pad3) -> Net-(U12-Rs)
- U7 pad 1: /Commutation/LAMP_OUT -> GND
- U7 pad 2: Net-(Q2-D) -> +3.3V
- U7 pad 3: +12V -> +5V
- U9 pad 1: GND -> /Platine2/CanTransceiver2/CAN_TX
- U9 pad 2: +5V -> GND
- U9 pad 4: /Commutation/SERVO_EN -> /Platine2/CanTransceiver2/CAN_RX
- U9 pad 5: /Commutation/OVER_CURR_SERVO -> unconnected-(U9-Vref-Pad5)
- U9 pad 6: /Commutation/SERVO_OUT -> /Platine2/CAN_L
- U9 pad 7: /Commutation/SERVO_OUT -> /Platine2/CAN_H
- U9 pad 8: /Commutation/SERVO_OUT -> Net-(U9-Rs)
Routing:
- net /I2C_SCL: track 92.0 -> 0.00 mm, vias 4 -> 0
- net /I2C_SDA: track 90.7 -> 0.00 mm, vias 4 -> 0
- net Net-(U5-2Y): track 81.9 -> 0.00 mm, vias 6 -> 0
- net Net-(U5-1Y): track 53.3 -> 0.00 mm, vias 2 -> 0
- net Net-(Q6-G): track 50.7 -> 0.00 mm, vias 2 -> 0
- net +12V: track 90.7 -> 42.9 mm, vias 27 -> 0
- net Net-(Q11-C): track 0.00 -> 46.4 mm
- net Net-(U37-1Y): track 0.00 -> 38.3 mm, vias 0 -> 2
- net Net-(U37-2Y): track 0.00 -> 37.3 mm, vias 0 -> 2
- net +5V: track 173.7 -> 138.5 mm, vias 7 -> 5
- net Net-(U15-1Y): track 32.6 -> 0.00 mm, vias 2 -> 0
- net /EN_MOTOR: track 31.4 -> 0.00 mm, vias 3 -> 0
- net /DIN: track 27.9 -> 0.00 mm, vias 3 -> 0
- net Net-(U12-Pad4): track 27.8 -> 0.00 mm, vias 2 -> 0
- net Net-(U15-2Y): track 27.7 -> 0.00 mm, vias 2 -> 0
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- added copper zone on F.Cu, net /Platine1/Commutation1-1/LAMP_OUT
- added copper zone on F.Cu, net /Platine1/Commutation1-1/POLE+
- added copper zone on F.Cu, net /Platine1/Commutation1-1/POLE-
- added copper zone on F.Cu, net /Platine1/Commutation1-1/SERVO_OUT
- added copper zone on F.Cu, net /Platine1/Protection1/12V_IN
- added copper zone on F.Cu, net /Platine1/Protection1/5V_IN
- added copper zone on F.Cu, net Net-(F2-Pad2)
- added copper zone on F.Cu, net Net-(J16-Pin_2)
- removed copper zone on In2.Cu, net +12V
- removed copper zone on F.Cu, net /Commutation/LAMP_OUT
- removed copper zone on F.Cu, net /Commutation/Motor_driver_1/POLE1
- removed copper zone on In2.Cu, net /Commutation/Motor_driver_1/POLE1
- removed copper zone on F.Cu, net /Commutation/Motor_driver_1/POLE2
- removed copper zone on F.Cu, net /Commutation/Motor_driver_2/POLE_1
- removed copper zone on F.Cu, net /Commutation/Motor_driver_2/POLE_2
- removed copper zone on F.Cu, net /Commutation/POLE+
- removed copper zone on F.Cu, net /Commutation/POLE-
- removed copper zone on F.Cu, net /Commutation/SERVO_OUT
- removed copper zone on F.Cu, net /Protection/12V_IN
- removed copper zone on F.Cu, net /Protection/5V_IN
- removed copper zone on F.Cu, net Net-(F1-Pad2)
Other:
- board size 150 x 100 mm -> 204 x 100 mm
